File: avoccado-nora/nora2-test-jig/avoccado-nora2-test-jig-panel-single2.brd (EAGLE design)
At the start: 25 x 24.5 mm, 24 parts

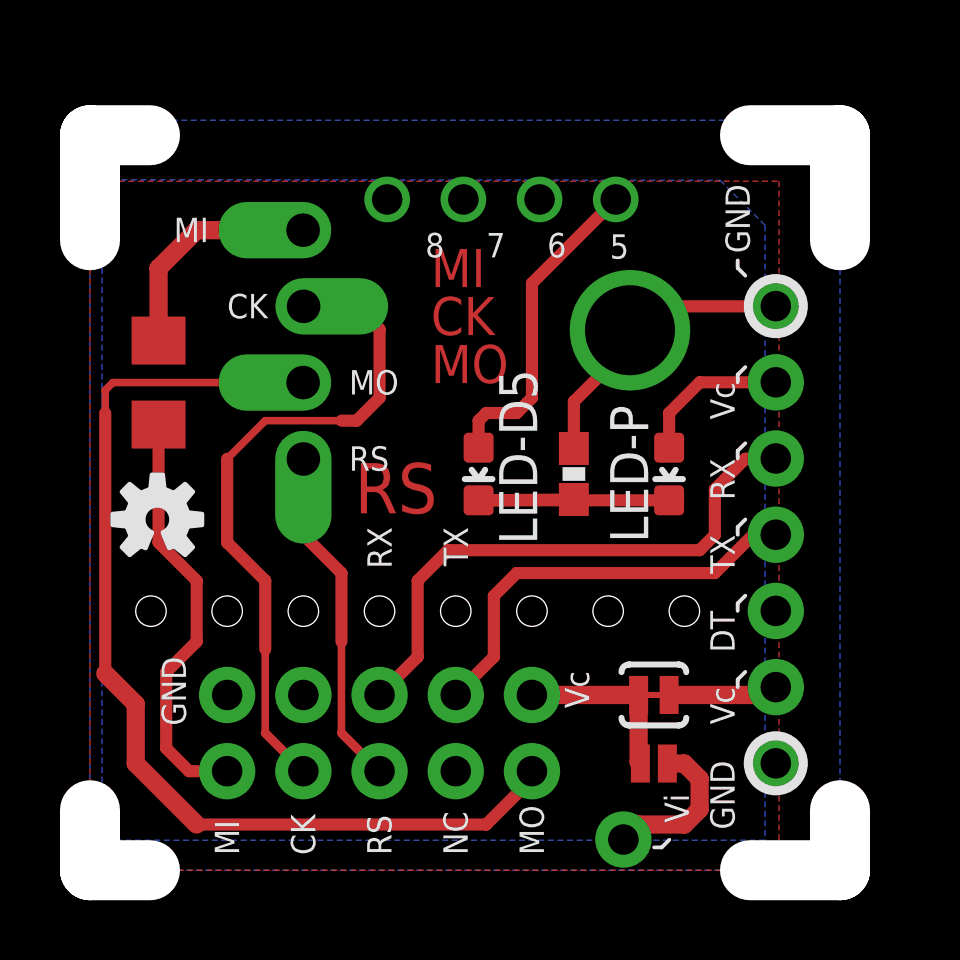
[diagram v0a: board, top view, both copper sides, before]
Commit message: bigger pads for test jig, g-code for solder stencils
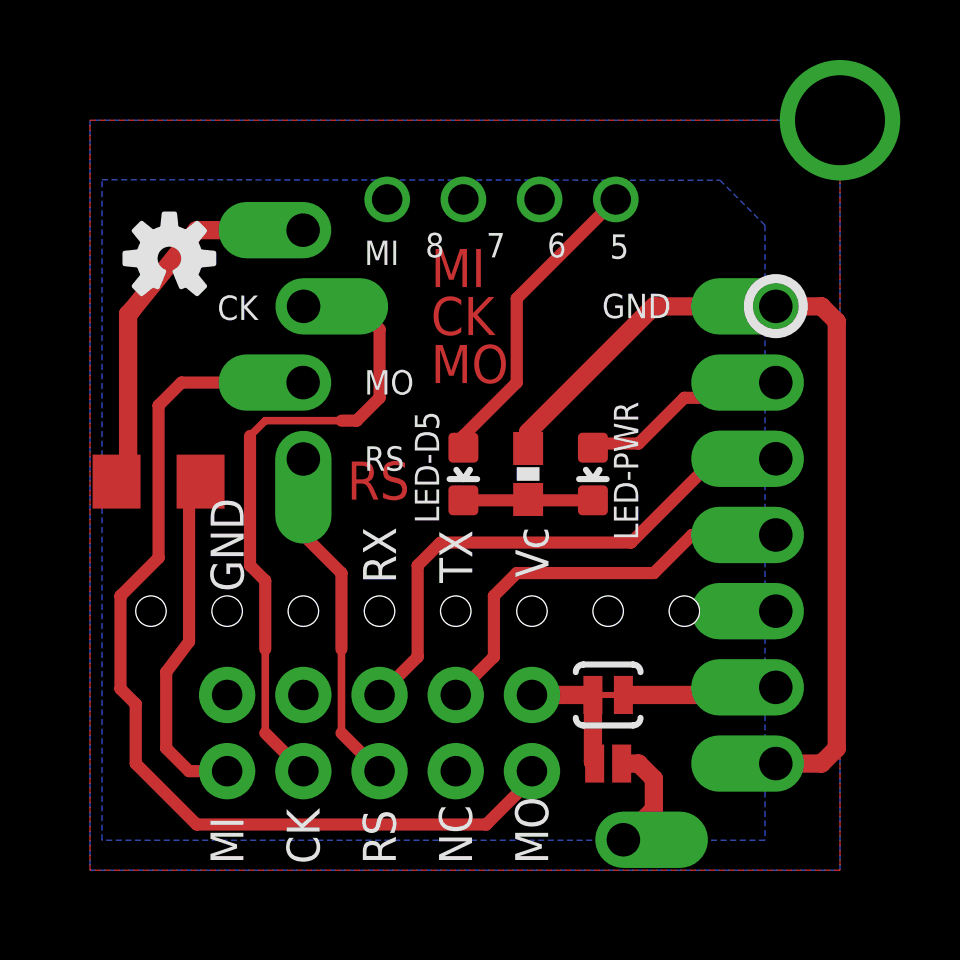
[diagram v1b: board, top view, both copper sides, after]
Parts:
- removed D5-LED, PWR-LED: (no value), SparkFun-LED:LED-0603
- removed JP10, JP11, JP17, JP18, JP3, JP6, JP8, JP9: M01PTH, SparkFun-Connectors:1X01
- added JP1, JP16, JP19, JP2, JP20, JP4, JP5, JP7: M01OFFSET, SparkFun-Connectors:1X01_OFFSET
- added LED-D5, LED-PWR: (no value), SparkFun-LED:LED-0603
- moved LOGO2 8.71 mm to (2.65, 20.4)
- moved R1 3.30 mm to (2.29, 13.0), turned to 0 degrees
- moved R2 1.52 mm to (14.6, 13.2)
- moved SJ1 1.52 mm to (17.3, 5.84)
- moved SJ2 1.52 mm to (17.3, 3.56)
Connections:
- net 3.3V: now also JP19.1; no longer JP18.1
- net 5V: now also JP16.1; no longer JP17.1
- net D5: now also LED-D5.A; no longer D5-LED.A
- net DTR: now also JP5.1; no longer JP10.1
- net GND: now also JP1.1, JP20.1; no longer JP3.1, JP6.1
- net N$1: now also LED-D5.C, LED-PWR.C; no longer D5-LED.C, PWR-LED.C
- net N$2: now also JP7.1, LED-PWR.A; no longer JP11.1, PWR-LED.A
- net RXI: now also JP2.1; no longer JP8.1
- net TXO: now also JP4.1; no longer JP9.1
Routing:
- net GND: track 9.61 -> 29.3 mm
- net N$1: track 9.50 -> 4.32 mm
- net MISO: track 7.75 -> 12.9 mm
- net MISO1: track 14.1 -> 11.6 mm
- net N$2: track 5.14 -> 7.00 mm
- net MOSI: track 34.5 -> 32.7 mm
- net VTG: track 5.87 -> 4.34 mm
- net 3.3V: track 3.66 -> 5.19 mm
- net 5V: track 5.26 -> 3.74 mm
- net SCK: track 22.5 -> 21.9 mm
- net RXI: track 18.8 -> 18.3 mm
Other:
- board outline removed
- board text removed: "LED-D5"
- board text removed: "LED-P"
